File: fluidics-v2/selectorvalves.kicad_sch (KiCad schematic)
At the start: 35 parts, among them IC1 MCZ33996EKR2

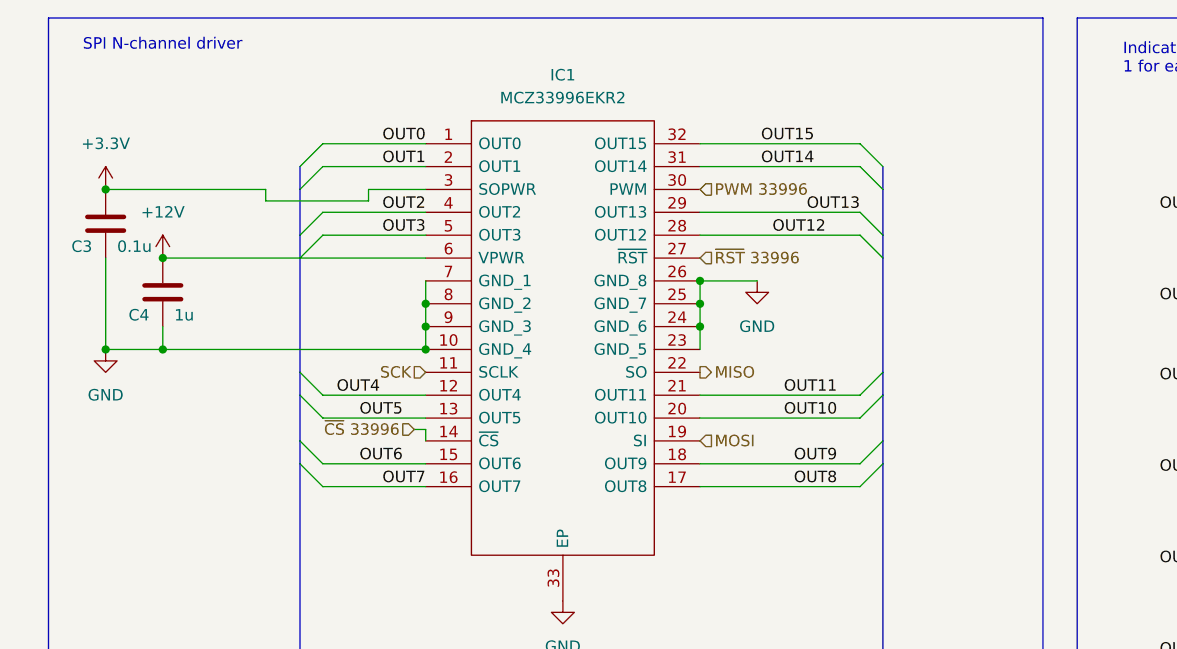
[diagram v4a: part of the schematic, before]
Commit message: added pullups/downs to spi for stability, rounded corners
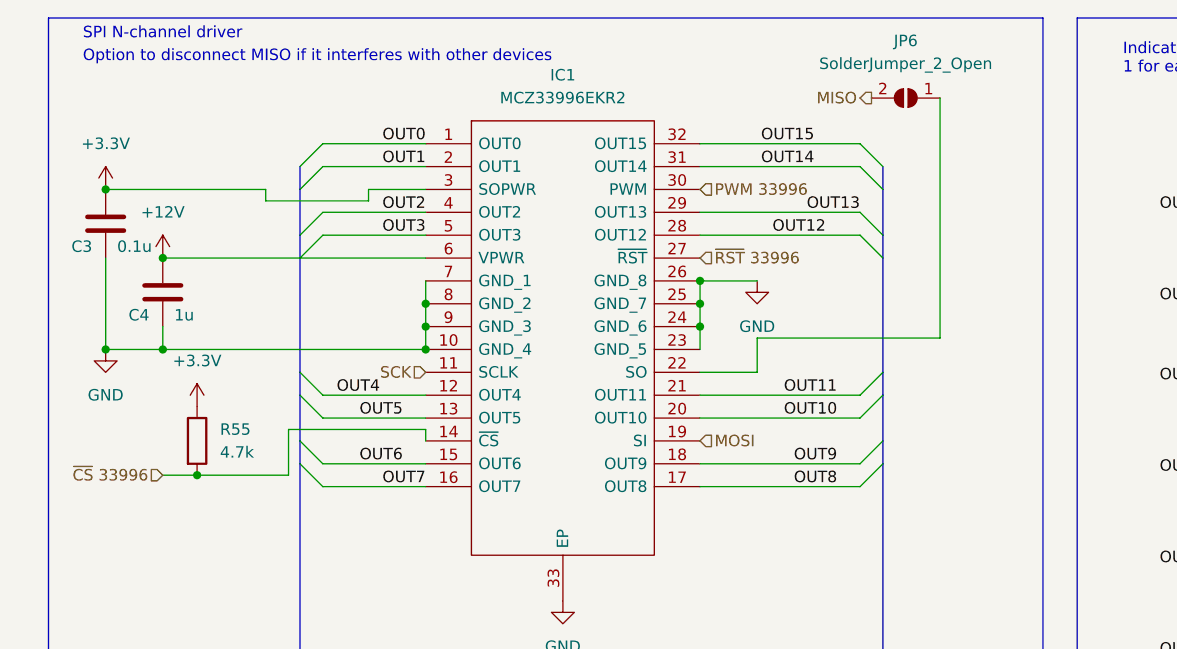
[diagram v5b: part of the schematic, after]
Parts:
- added JP6: SolderJumper_2_Open, Jumper:SolderJumper-2_P1.3mm_Open_TrianglePad1.0x1.5mm, symbol Jumper:SolderJumper_2_Open
- added R55: 4.7k, Resistor_SMD:R_0402_1005Metric, symbol Device:R
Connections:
- net +3.3V: now also R55.1
- net MISO: now also JP6.2 (B); no longer IC1.22 (SO)
- net ~{CS} 33996: now also R55.2
- new net: IC1.22 (SO), JP6.1 (A)
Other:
- note added: "Option to disconnect MISO if it interferes with other devices"
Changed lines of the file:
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@@
   (junction (at 160.02 86.36) (diameter 0) (color 0 0 0 0)
   )
+  (junction (at 31.75 66.04) (diameter 0) (color 0 0 0 0)
+  )
   (junction (at 160.02 153.67) (diameter 0) (color 0 0 0 0)
   )
@@
     (stroke (width 0) (type default))
   )
+  (wire (pts (xy 114.3 24.13) (xy 114.3 50.8))
+    (stroke (width 0) (type default))
+  )
   (wire (pts (xy 160.02 153.67) (xy 160.02 163.83))
     (stroke (width 0) (type default))
@@
     (stroke (width 0) (type default))
   )
+  (wire (pts (xy 27.94 66.04) (xy 31.75 66.04))
+    (stroke (width 0) (type default))
+  )
   (wire (pts (xy 160.02 181.61) (xy 158.75 181.61))
     (stroke (width 0) (type default))
@@
     (stroke (width 0) (type default))
   )
+  (wire (pts (xy 93.98 54.61) (xy 87.63 54.61))
+    (stroke (width 0) (type default))
+  )
   (wire (pts (xy 27.94 49.53) (xy 27.94 52.07))
     (stroke (width 0) (type default))
@@
     (stroke (width 0) (type default))
   )
+  (wire (pts (xy 41.91 66.04) (xy 41.91 60.96))
+    (stroke (width 0) (type default))
+  )
   (bus (pts (xy 43.18 62.23) (xy 43.18 64.77))
     (stroke (width 0) (type default))
@@
     (stroke (width 0) (type default))
   )
+  (wire (pts (xy 93.98 50.8) (xy 93.98 54.61))
+    (stroke (width 0) (type default))
+  )
   (bus (pts (xy 43.18 31.75) (xy 43.18 34.29))
     (stroke (width 0) (type default))
@@
     (stroke (width 0) (type default))
   )
+  (wire (pts (xy 31.75 66.04) (xy 41.91 66.04))
+    (stroke (width 0) (type default))
+  )
   (wire (pts (xy 87.63 57.15) (xy 105.41 57.15))
     (stroke (width 0) (type default))
@@
     (stroke (width 0) (type default))
   )
-  (wire (pts (xy 57.15 60.96) (xy 55.88 60.96))
+  (wire (pts (xy 57.15 60.96) (xy 41.91 60.96))
     (stroke (width 0) (type default))
   )
@@
     (stroke (width 0) (type default))
   )
+  (wire (pts (xy 93.98 50.8) (xy 114.3 50.8))
+    (stroke (width 0) (type default))
+  )
   (wire (pts (xy 160.02 114.3) (xy 158.75 114.3))
     (stroke (width 0) (type default))
@@
     (fill (type none))
   )
-  (text "SPI N-channel driver" (at 19.05 19.05 0)
+  (text "Option to disconnect MISO if it interferes with other devices"
+    (at 19.05 20.32 0)
+    (effects (font (size 1.27 1.27)) (justify left bottom))
+  )
+  (text "SPI N-channel driver" (at 19.05 17.78 0)
     (effects (font (size 1.27 1.27)) (justify left bottom))
   )
@@
     (effects (font (size 1.27 1.27)) (justify right bottom))
   )
+  (hierarchical_label "MISO" (shape output) (at 106.68 24.13 180) (fields_autoplaced)
+    (effects (font (size 1.27 1.27)) (justify right))
+  )
   (hierarchical_label "~{RST} 33996" (shape input) (at 87.63 41.91 0) (fields_autoplaced)
     (effects (font (size 1.27 1.27)) (justify left))
   )
-  (hierarchical_label "MISO" (shape output) (at 87.63 54.61 0) (fields_autoplaced)
-    (effects (font (size 1.27 1.27)) (justify left))
-  )
   (hierarchical_label "MOSI" (shape input) (at 87.63 62.23 0) (fields_autoplaced)
     (effects (font (size 1.27 1.27)) (justify left))
   )
-  (hierarchical_label "~{CS} 33996" (shape input) (at 55.88 60.96 180) (fields_autoplaced)
-    (effects (font (size 1.27 1.27)) (justify right))
-  )
   (hierarchical_label "PWM 33996" (shape input) (at 87.63 34.29 0) (fields_autoplaced)
     (effects (font (size 1.27 1.27)) (justify left))
@@
     (effects (font (size 1.27 1.27)) (justify left))
   )
+  (hierarchical_label "~{CS} 33996" (shape input) (at 27.94 66.04 180) (fields_autoplaced)
+    (effects (font (size 1.27 1.27)) (justify right))
+  )
   (symbol (lib_id "Device:LED") (at 154.94 55.88 0) (unit 1)
     (in_bom yes) (on_board yes) (dnp no)
@@
         (path "/8147bc74-d9d4-4f1e-bd7d-8bc37b8b3806/00000000-0000-0000-0000-0000600fc6db"
           (reference "D?") (unit 1)
+        )
+      )
+    )
+  )
+  (symbol (lib_id "Device:R") (at 31.75 62.23 0) (unit 1)
+    (in_bom yes) (on_board yes) (dnp no) (fields_autoplaced)
+    (property "Reference" "R55" (at 34.29 60.96 0)
+      (effects (font (size 1.27 1.27)) (justify left))
+    )
+    (property "Value" "4.7k" (at 34.29 63.5 0)
+      (effects (font (size 1.27 1.27)) (justify left))
+    )
+    (property "Footprint" "Resistor_SMD:R_0402_1005Metric" (at 29.972 62.23 90)
+      (effects (font (size 1.27 1.27)) hide)
+    )
+    (property "Datasheet" "~" (at 31.75 62.23 0)
+      (effects (font (size 1.27 1.27)) hide)
+    )
+    (pin "1")
+    (pin "2")
+    (instances
+      (project "fluidics-v2"
+        (path "/0ec91c42-8aad-437d-8c85-5e10f0e51fe0/c1c30de3-a3db-48df-8d6b-b2f91b9251f0"
+          (reference "R55") (unit 1)
         )
       )
@@
     )
   )
+  (symbol (lib_id "power:+3.3V") (at 31.75 58.42 0) (unit 1)
+    (in_bom yes) (on_board yes) (dnp no) (fields_autoplaced)
+    (property "Reference" "#PWR0160" (at 31.75 62.23 0)
+      (effects (font (size 1.27 1.27)) hide)
+    )
+    (property "Value" "+3.3V" (at 31.75 53.34 0)
+      (effects (font (size 1.27 1.27)))
+    )
+    (property "Footprint" "" (at 31.75 58.42 0)
+      (effects (font (size 1.27 1.27)) hide)
+    )
+    (property "Datasheet" "" (at 31.75 58.42 0)
+      (effects (font (size 1.27 1.27)) hide)
+    )
+    (pin "1")
+    (instances
+      (project "fluidics-v2"
+        (path "/0ec91c42-8aad-437d-8c85-5e10f0e51fe0/c1c30de3-a3db-48df-8d6b-b2f91b9251f0"
+          (reference "#PWR0160") (unit 1)
+        )
+      )
+    )
+  )
   (symbol (lib_id "Device:LED") (at 154.94 104.14 0) (unit 1)
     (in_bom yes) (on_board yes) (dnp no)
@@
         )
       )
+    )
+  )
+  (symbol (lib_id "Jumper:SolderJumper_2_Open") (at 110.49 24.13 180) (unit 1)
+    (in_bom yes) (on_board yes) (dnp no) (fields_autoplaced)
+    (property "Reference" "JP6" (at 110.49 17.78 0)
+      (effects (font (size 1.27 1.27)))
+    )
+    (property "Value" "SolderJumper_2_Open" (at 110.49 20.32 0)
+      (effects (font (size 1.27 1.27)))
+    )
+    (property "Footprint" "Jumper:SolderJumper-2_P1.3mm_Open_TrianglePad1.0x1.5mm" (at 110.49 24.13 0)
+      (effects (font (size 1.27 1.27)) hide)
+    )
+    (property "Datasheet" "~" (at 110.49 24.13 0)
+      (effects (font (size 1.27 1.27)) hide)
+    )
+    (pin "1")
+    (pin "2")
+    (instances
+      (project "fluidics-v2"
+        (path "/0ec91c42-8aad-437d-8c85-5e10f0e51fe0/c1c30de3-a3db-48df-8d6b-b2f91b9251f0"
+          (reference "JP6") (unit 1)
+        )
+      )
